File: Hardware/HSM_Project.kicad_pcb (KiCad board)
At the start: 2 copper layers, 97 x 100.8 mm, 100 parts, among them J1 Conn_01x02_Pin, J10 VL530X Connector, J11 VL530X Connector, J12 VL530X Connector, J13 VL530X Connector, J16 HC-05 Breakout Board, J17 Conn_01x04_Pin, J18 Conn_01x02_Pin, J19 Conn_01x02_Pin, J2 MP1584 Breakout, J20 Conn_01x04_Pin, J3 DRV8833 Breakout, J4 TEENSY_4.1, J5 BNO055 Breakout, J8 VL530X Connector, J9 VL530X Connector, Q10 Q_NMOS_GSD, Q11 Q_NMOS_GSD, Q12 Q_NMOS_GSD, Q13 TEFT4300, Q2 Q_NMOS_GSD, Q3 TEFT4300, Q4 TEFT4300, Q5 TEFT4300, Q6 TEFT4300, Q7 TEFT4300, Q8 Q_NMOS_GSD, Q9 Q_NMOS_GSD, SW1 SW_SPDT, SW2 SW_SPDT, SW3 SW_Push, SW4 SW_Push

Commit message: Final updated pcb and schematic before dfm check
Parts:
- removed J17, J20: Conn_01x04_Pin, Connector_JST:JST_PH_B4B-PH-K_1x04_P2.00mm_Vertical
- removed J18, J19: Conn_01x02_Pin, Connector_JST:JST_PH_B2B-PH-K_1x02_P2.00mm_Vertical
- added F1: Fuse, Fuse:Fuse_1206_3216Metric_Pad1.42x1.75mm_HandSolder, B.Cu at (137.8, 114.5)
- added G***: LOGO, LOGO, F.Cu at (153.8, 44.1)
- added H10: MountingHole, MountingHole:MountingHole_2mm, F.Cu at (153.8, 22.4)
- added H5: MountingHole, MountingHole:MountingHole_2mm, F.Cu at (132.0, 101.7)
- added H6: MountingHole, MountingHole:MountingHole_2mm, F.Cu at (132.0, 119.4)
- added H7: MountingHole, MountingHole:MountingHole_2mm, F.Cu at (175.1, 101.7)
- added H8: MountingHole, MountingHole:MountingHole_2mm, F.Cu at (175.1, 119.4)
- added H9: MountingHole, MountingHole:MountingHole_2mm, F.Cu at (153.8, 37.4)
- added J14: BNO085 Breakout, Micromouse_Footprints:BNO085, F.Cu at (153.7, 61.2)
- added J6: Conn_01x06_Pin, Connector_PinHeader_2.54mm:PinHeader_1x06_P2.54mm_Vertical, F.Cu at (142.5, 95.3)
- added J7: Conn_01x06_Pin, Connector_PinHeader_2.54mm:PinHeader_1x06_P2.54mm_Vertical, F.Cu at (163.8, 95.3)
- C1, C10, C11, C12, C13, C16, C17, C2, C21, C22, C3, C4, C5, C6, C7, C8, C9: footprint Capacitor_SMD:C_0603_1608Metric -> Capacitor_SMD:C_0603_1608Metric_Pad1.08x0.95mm_HandSolder
- D1, D4, D6, D7, D8, D9: footprint LED_THT:LED_D5.0mm -> SFH_4545:DIO_SFH_4545
- D2: footprint Diode_SMD:D_SMA -> Diode_SMD:D_SMA_Handsoldering
- D3: footprint LED_SMD:LED_0603_1608Metric -> LED_THT:LED_D3.0mm
- J1: footprint Connector_JST:JST_XH_B2B-XH-A_1x02_P2.50mm_Vertical -> Connector_AMASS:AMASS_XT60-M_1x02_P7.20mm_Vertical
- J5: value BNO055 Breakout -> Conn_01x08_Pin; footprint Micromouse_Footprints:BNO055 -> Connector_PinSocket_2.54mm:PinSocket_1x08_P2.54mm_Vertical
- Q13, Q3, Q4, Q5, Q6, Q7: footprint LED_THT:LED_D3.0mm -> TEFT4300 (2):XDCR_TEFT4300
- R1, R10, R11, R12, R13, R14, R15, R17, R19, R2, R20, R21, R22, R23, R24, R25, R26, R27, R28, R29, R30, R31, R32, R33, R34, R35, R36, R37, R38, R4, R5, R6, R7, R8, R9: footprint Resistor_SMD:R_0603_1608Metric -> Resistor_SMD:R_0603_1608Metric_Pad0.98x0.95mm_HandSolder
- R16, R18: footprint Resistor_SMD:R_0603_1608Metric -> Resistor_SMD:R_0603_1608Metric_Pad0.98x0.95mm_HandSolder; moved to B.Cu
- R3: footprint Resistor_SMD:R_0603_1608Metric -> Resistor_SMD:R_0603_1608Metric_Pad0.98x0.95mm_HandSolder; moved to F.Cu
- SW1, SW2: footprint Button_Switch_SMD:SW_SPDT_CK_JS102011SAQN -> Button_Switch_THT:SW_Slide_SPDT_Angled_CK_OS102011MA1Q
- SW3, SW4: footprint Button_Switch_SMD:SW_SPST_TL3342 -> Button_Switch_THT:SW_PUSH_6mm_H5mm
- moved SW1 79.1 mm to (116.4, 94.8), turned to -90 degrees
- moved C17 63.1 mm to (186.4, 120.8)
- moved R33 62.9 mm to (182.3, 114.7)
- moved R1 62.8 mm to (180.1, 114.7)
- moved C16 62.6 mm to (177.9, 114.7)
- moved R27 62.2 mm to (188.5, 120.9)
- moved R2 61.2 mm to (190.5, 120.9)
- moved SW3 58.0 mm to (185.2, 124.4)
- moved SW4 57.4 mm to (175.5, 124.4)
- moved SW2 53.7 mm to (117.0, 122.9), turned to -90 degrees
- moved R6 52.6 mm to (149.6, 125.6), turned to 90 degrees
- moved C8 50.2 mm to (151.7, 125.6), turned to -90 degrees
- moved R7 48.0 mm to (153.7, 125.6), turned to 90 degrees
- moved D3 40.2 mm to (194.1, 89.0), turned to 180 degrees
- moved R3 35.4 mm to (188.1, 89.0)
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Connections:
- C1 pad 1: /Control Unit/VOUT -> +5V
- C10 pad 1: IN+ -> Net-(D2-K)
- C11 pad 1: /Control Unit/VOUT -> +5V
- C12 pad 1: /Control Unit/VOUT -> +5V
- C13 pad 1: /Control Unit/VOUT -> +5V
- C2 pad 1: /Control Unit/VOUT -> +5V
- C3 pad 1: /Control Unit/VOUT -> +5V
- C4 pad 1: /Control Unit/VOUT -> +5V
- C5 pad 1: /Control Unit/VOUT -> +5V
- D2 pad 2: /Power Unit/VBAT -> Net-(D2-A)
- J1 pad 1: /Power Unit/VBAT -> Net-(J1-Pin_1)
- J10 pad 1: /Control Unit/VOUT -> +5V
- J11 pad 1: /Control Unit/VOUT -> +5V
- J12 pad 1: /Control Unit/VOUT -> +5V
- J13 pad 1: /Control Unit/VOUT -> +5V
- J16 pad 2: /Control Unit/VOUT -> +5V
- J2 pad 1: IN+ -> VBAT
- J2 pad 2: IN+ -> VBAT
- J2 pad 7: /Control Unit/VOUT -> +5V
- J2 pad 8: /Control Unit/VOUT -> +5V
- J4 pad D11: unconnected-(J4-(SDO)D11-PadD11) -> /Control Unit/RST_GPIO
- J4 pad D26: unconnected-(J4-A12-PadD26) -> /Control Unit/INT_GPIO
- J4 pad VIN: /Control Unit/VOUT -> +5V
- J5 pad 1: /Control Unit/VOUT -> +3.3V
- J5 pad 2: unconnected-(J5-3.3V-Pad2) -> GND
- J5 pad 3: GND -> /Control Unit/SCL1
- J5 pad 5: /Control Unit/SCL1 -> unconnected-(J5-Pin_5-Pad5)
- J5 pad 8: GND -> /Control Unit/INT_GPIO
- J8 pad 1: /Control Unit/VOUT -> +5V
- J9 pad 1: /Control Unit/VOUT -> +5V
- R16 pad 1: /Control Unit/VOUT -> +5V
- R18 pad 1: /Control Unit/VOUT -> +5V
- R20 pad 1: /Control Unit/VOUT -> +5V
- R22 pad 1: /Control Unit/VOUT -> +5V
- R29 pad 1: /Control Unit/VOUT -> +5V
- R3 pad 1: /Control Unit/VOUT -> +5V
- R6 pad 1: IN+ -> VBAT
- R8 pad 1: /Control Unit/VOUT -> +5V
- SW1 pad 2: IN+ -> VBAT
- SW2 pad 3: IN+ -> VBAT
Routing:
- net /Control Unit/VOUT: track 310.2 -> 0.00 mm, vias 15 -> 0
- net +5V: track 0.00 -> 308.9 mm, vias 0 -> 8
- net IN+: track 108.0 -> 0.00 mm, vias 1 -> 0
- net VBAT: track 0.00 -> 72.1 mm
- net /Control Unit/INT_GPIO: track 0.00 -> 57.8 mm, vias 0 -> 2
- net GND: track 105.4 -> 153.4 mm, vias 12 -> 19
- net /Control Unit/RST_GPIO: track 0.00 -> 40.5 mm, vias 0 -> 3
- net /Control Unit/VBAT_MONITOR: track 13.0 -> 53.4 mm, vias 0 -> 1
- net /Control Unit/ALGO_CONTROL: track 74.4 -> 40.7 mm, vias 1 -> 0
- net /Control Unit/SCL1: track 84.1 -> 113.2 mm, vias 0 -> 4
- net /Control Unit/SDA1: track 85.1 -> 113.4 mm, vias 0 -> 2
- net /Control Unit/RUN_MODE_GPIO: track 59.0 -> 39.1 mm
- net /Control Unit/ENC2_B: track 5.77 -> 22.8 mm, vias 0 -> 1
- net Net-(D2-K): track 21.1 -> 38.1 mm
- net /Control Unit/ENC1_A: track 5.84 -> 21.9 mm, vias 0 -> 1
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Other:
- board size 97 x 100.8 mm -> 97 x 111 mm

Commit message: Ignore KiCad .history folder
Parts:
- removed R1, R27: 1k, Resistor_SMD:R_0603_1608Metric_Pad0.98x0.95mm_HandSolder
- added G***: LOGO, LOGO, F.Cu at (186.4, 95.9)
- H1, H10, H2, H3, H4, H5, H6, H7, H8, H9: footprint MountingHole:MountingHole_2mm -> MountingHole:MountingHole_2.1mm
- J14: footprint Micromouse_Footprints:BNO085 -> Micromouse:BNO085
- J2: footprint Micromouse_Footprints:SRT_MPT1584EN_Module -> Micromouse:MP1584
- J3: footprint Micromouse_Footprints:DRV8833 -> Micromouse:DRV8833
- R16, R18, R20, R22, R29, R8: value 33 -> 39
- R3: moved to B.Cu
- SW3, SW4: footprint Button_Switch_THT:SW_PUSH_6mm_H5mm -> Micromouse:Rectangular Tact Button
- moved D3 44.3 mm to (173.3, 128.1), turned to 0 degrees
- moved R3 38.1 mm to (174.6, 124.6)
- moved SW4 12.4 mm to (187.1, 128.6)
- moved C16 11.8 mm to (180.8, 126.1)
- moved R33 11.4 mm to (183.0, 126.1)
- moved R2 5.37 mm to (186.1, 123.9), turned to 90 degrees
- moved C17 3.55 mm to (188.2, 123.9), turned to 90 degrees
- moved J2 2.98 mm to (152.3, 121.2)
- moved SW1 2.93 mm to (119.4, 94.8)
- moved SW2 2.33 mm to (119.3, 123.4)
- moved D5 2.08 mm to (167.9, 127.5)
- moved R4 1.97 mm to (170.5, 122.8)
- moved SW3 1.90 mm to (187.1, 124.5), turned to 180 degrees
- moved C9 1.29 mm to (166.2, 122.9)
- moved G*** 1.27 mm to (153.8, 42.8)
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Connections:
- C16 pad 1: /Control Unit/RUN_MODE_GPIO -> GND
- C16 pad 2: GND -> /Control Unit/RUN_MODE_GPIO
- C17 pad 1: /Control Unit/ALGO_CONTROL -> GND
- C17 pad 2: GND -> /Control Unit/ALGO_CONTROL
- J10 pad 3: /Control Unit/SDA1 -> /Control Unit/SCL1
- J10 pad 4: /Control Unit/SCL1 -> /Control Unit/SDA1
- J11 pad 3: /Control Unit/SDA1 -> /Control Unit/SCL1
- J11 pad 4: /Control Unit/SCL1 -> /Control Unit/SDA1
- J12 pad 3: /Control Unit/SDA0 -> /Control Unit/SCL0
- J12 pad 4: /Control Unit/SCL0 -> /Control Unit/SDA0
- J13 pad 3: /Control Unit/SDA0 -> /Control Unit/SCL0
- J13 pad 4: /Control Unit/SCL0 -> /Control Unit/SDA0
- J8 pad 3: /Control Unit/SDA1 -> /Control Unit/SCL1
- J8 pad 4: /Control Unit/SCL1 -> /Control Unit/SDA1
- J9 pad 3: /Control Unit/SDA0 -> /Control Unit/SCL0
- J9 pad 4: /Control Unit/SCL0 -> /Control Unit/SDA0
- R2 pad 2: Net-(R2-Pad2) -> /Control Unit/ALGO_CONTROL
- R33 pad 2: Net-(R1-Pad2) -> /Control Unit/RUN_MODE_GPIO
- SW3 pad 1: Net-(R2-Pad2) -> /Control Unit/ALGO_CONTROL
- SW4 pad 1: Net-(R1-Pad2) -> /Control Unit/RUN_MODE_GPIO
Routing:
- net +3.3V: track 333.8 -> 308.2 mm
- net Net-(R1-Pad2): track 18.5 -> 0.00 mm
- net /Control Unit/RUN_MODE_GPIO: track 39.1 -> 55.7 mm, vias 1 -> 2
- net GND: track 153.4 -> 138.7 mm, vias 19 -> 80
- net +5V: track 308.9 -> 322.6 mm, vias 8 -> 7
- net Net-(R2-Pad2): track 13.2 -> 0.00 mm, vias 1 -> 0
- net /Control Unit/SCL0: track 72.2 -> 65.4 mm
- net /Control Unit/VBAT_MONITOR: track 53.4 -> 48.1 mm
- net /Control Unit/SDA0: track 70.6 -> 74.6 mm, vias 1 -> 3
- net /Control Unit/ALGO_CONTROL: track 40.7 -> 44.2 mm, vias 0 -> 1
- net /Control Unit/SCL1: track 113.2 -> 110.1 mm, vias 4 -> 2
- net Net-(J3-VCC): track 44.0 -> 41.0 mm
- net /Control Unit/INT_GPIO: track 57.8 -> 54.7 mm, vias 2 -> 3
- net /Control Unit/SDA1: track 113.4 -> 116.4 mm, vias 2 -> 4
- net /Control Unit/RST_GPIO: track 40.5 -> 43.2 mm, vias 3 -> 1
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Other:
- board size 97 x 111 mm -> 97 x 111.3 mm
- board text added: "ALGO SWITCH"
- board text added: "BATCH:RM16"
- board text added: "BATTERY KILL SWITCH"
- board text added: "BATTERY MONITOR LED"
- board text added: "BNO085"
- board text added: "CONTRIBUTORS: DAIVIK NEOGI SUTEJ SHETTY KAPILMEET SINGH"
- board text added: "DESIGNED TIMELINE:MAY 2026"
- board text added: "DRV8833"
- board text added: "EMITTER"
- board text added: "ENCODER+MOTOR OUTPUT"
- board text added: "HC-05"
- board text added: "MOTOR KILL SWITCH"
- board text added: "MPU6050"
- board text added: "N20-MOTORS"
- board text added: "POWER INDICATION LED"
- board text added: "RECIEVER"
- board text added: "RUNMODE SWITCH"
- board text added: "XT60"

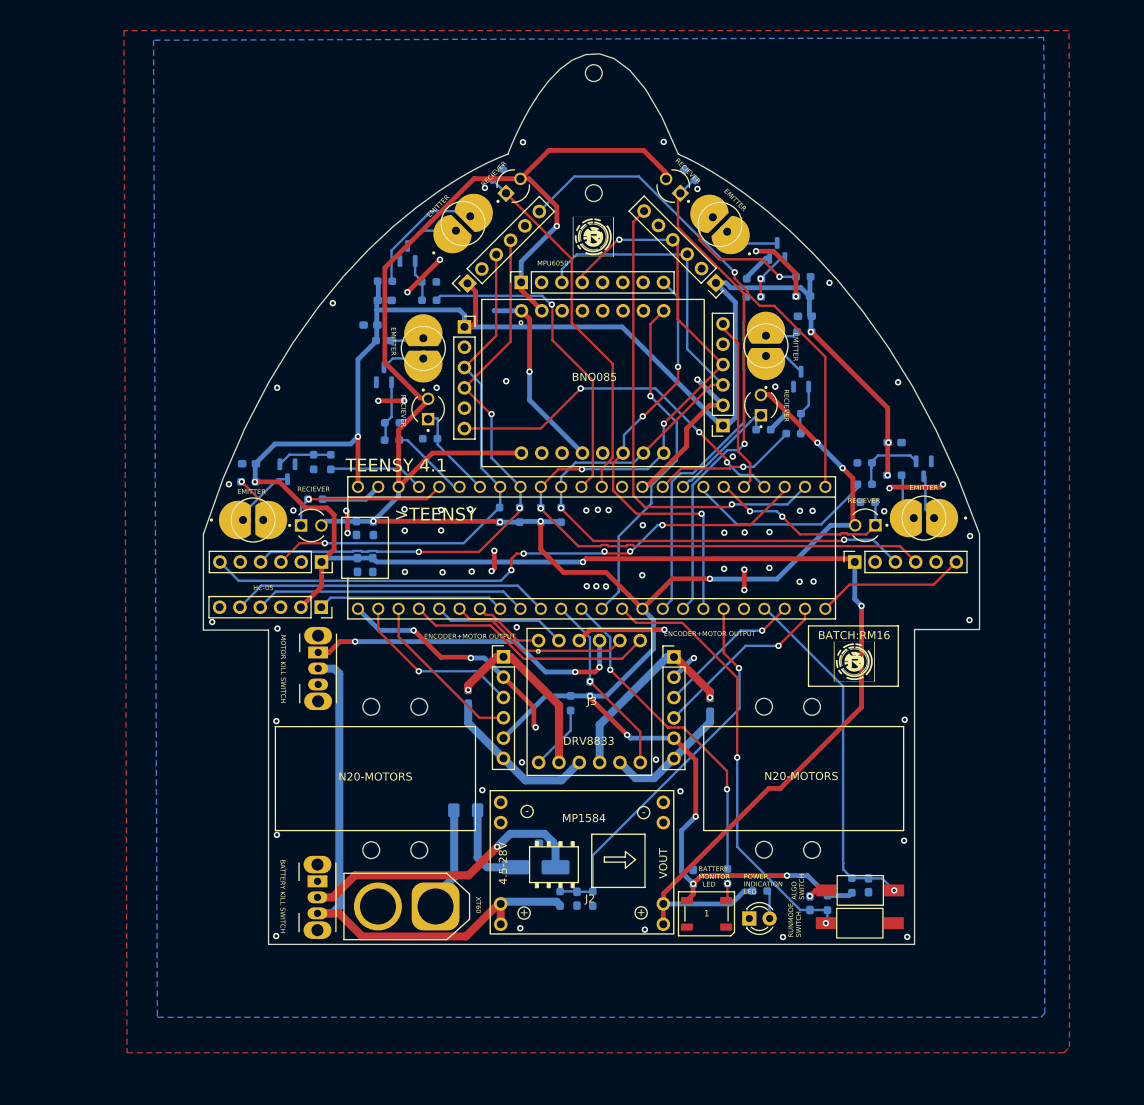
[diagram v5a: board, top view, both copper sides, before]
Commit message: updated the dimensiosn of tb6612,shifted placements based on dfm check, other changes
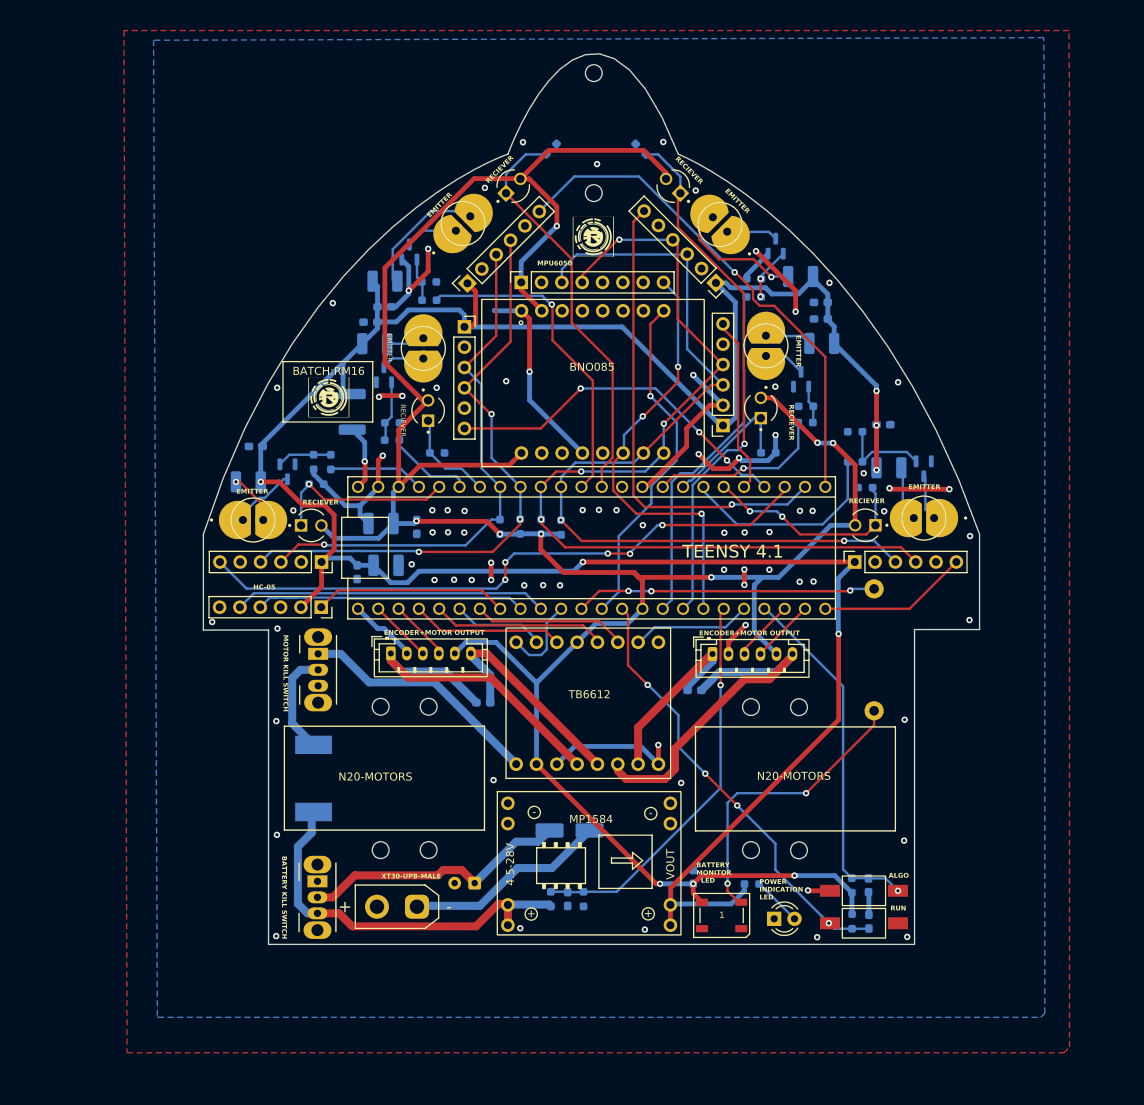
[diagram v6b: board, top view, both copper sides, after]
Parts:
- removed F1: Fuse, Fuse:Fuse_1206_3216Metric_Pad1.42x1.75mm_HandSolder
- removed J3: DRV8833 Breakout, Micromouse:DRV8833
- removed R25, R26: 10k, Resistor_SMD:R_0603_1608Metric_Pad0.98x0.95mm_HandSolder
- removed SW1: SW_SPDT, Button_Switch_THT:SW_Slide_SPDT_Angled_CK_OS102011MA1Q
- added F2: Polyfuse, Fuse:Fuse_Bourns_MF-SM_9.5x6.71mm, B.Cu at (118.8, 110.5)
- added F3: Polyfuse, Fuse:Fuse_1812_4532Metric_Pad1.30x3.40mm_HandSolder, B.Cu at (123.6, 64.7)
- added SW5: SW_SPDT, Button_Switch_THT:SW_Slide_SPDT_Angled_CK_OS102011MA1Q, F.Cu at (119.4, 95.0)
- added TB1: ~, TB6612:TB6612 module, F.Cu at (153.0, 102.9)
- C10: footprint Capacitor_SMD:C_0603_1608Metric_Pad1.08x0.95mm_HandSolder -> Capacitor_THT:CP_Radial_D6.3mm_P2.50mm
- C5, C7: footprint Capacitor_SMD:C_0603_1608Metric_Pad1.08x0.95mm_HandSolder -> Capacitor_SMD:C_1210_3225Metric_Pad1.33x2.70mm_HandSolder
- J1: footprint Connector_AMASS:AMASS_XT60-M_1x02_P7.20mm_Vertical -> Connector_AMASS:AMASS_XT30UPB-M_1x02_P5.0mm_Vertical
- J6, J7: footprint Connector_PinHeader_2.54mm:PinHeader_1x06_P2.54mm_Vertical -> Connector_JST:JST_PH_B6B-PH-K_1x06_P2.00mm_Vertical
- R16, R18, R20, R22, R29, R8: value 39 -> 36.5; footprint Resistor_SMD:R_0603_1608Metric_Pad0.98x0.95mm_HandSolder -> Resistor_SMD:R_1210_3225Metric_Pad1.30x2.65mm_HandSolder
- R4: footprint Resistor_SMD:R_0603_1608Metric_Pad0.98x0.95mm_HandSolder -> Resistor_THT:R_Axial_DIN0414_L11.9mm_D4.5mm_P15.24mm_Horizontal
- moved G*** 73.5 mm to (120.7, 62.9)
- moved R4 40.3 mm to (188.9, 86.8)
- moved J6 14.1 mm to (128.4, 94.9)
- moved C10 10.2 mm to (138.9, 123.6)
- moved C16 7.72 mm to (188.2, 128.4)
- moved R11 7.43 mm to (148.5, 31.9)
- moved R12 6.89 mm to (159.7, 31.9)
- moved D2 6.26 mm to (150.8, 117.0), turned to 0 degrees
- moved C6 5.42 mm to (131.7, 79.1)
- moved J7 4.83 mm to (168.7, 95.0)
- moved R32 4.07 mm to (186.5, 67.2)
- moved R33 3.86 mm to (186.1, 128.4)
- moved C7 3.11 mm to (127.2, 78.7), turned to 180 degrees
- moved D3 3.11 mm to (176.4, 128.1)
- moved R9 3.05 mm to (186.5, 71.0)
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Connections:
- J1 pad 1: Net-(J1-Pin_1) -> Net-(D2-A)
- J4 pad D28: unconnected-(J4-PadD28) -> PWMB
- J4 pad D9: /Control Unit/FAULT -> PWMA
- J4 pad VIN: +5V -> Net-(F3-Pad2)
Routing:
- net Net-(J3-VCC): track 41.0 -> 0.00 mm, vias 3 -> 0
- net Net-(D5-DIN): track 2.21 -> 37.5 mm, vias 1 -> 2
- net Net-(SW5-A): track 0.00 -> 30.5 mm
- net /Power Unit/M2_OUT2: track 16.3 -> 44.9 mm
- net /Control Unit/FAULT: track 23.8 -> 0.00 mm, vias 1 -> 0
- net VBAT: track 71.4 -> 49.2 mm
- net +3.3V: track 308.2 -> 328.8 mm, vias 12 -> 10
- net /Power Unit/M1_OUT1: track 23.1 -> 43.3 mm, vias 1 -> 0
- net GND: track 138.7 -> 155.2 mm, vias 80 -> 77
- net /Control Unit/ENC2_B: track 22.8 -> 7.95 mm, vias 1 -> 0
- net PWMB: track 0.00 -> 14.8 mm
- net Net-(D2-A): track 11.2 -> 25.5 mm
- net /Control Unit/ENC1_A: track 21.9 -> 7.89 mm, vias 1 -> 0
- net /Control Unit/ENC1_B: track 20.8 -> 7.66 mm
- net Net-(SW5-B): track 0.00 -> 13.1 mm
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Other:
- board text added: "ALGO"
- board text added: "RUN"
- board text added: "TB6612"
- board text added: "XT30-UPB-MALE"
- board text removed: "ALGO SWITCH"
- board text removed: "DRV8833"
- board text removed: "RUNMODE SWITCH"
- board text removed: "XT60"
